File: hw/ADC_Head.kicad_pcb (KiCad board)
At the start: 2 copper layers, 10 x 22 mm, 14 parts, among them J6 SMA HEAD OUT, U8 OPA365

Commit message: Head: + wire pad on the centre line (sets the piezo position), Auselia mark on the back; manual section 10 (questions and answers), clearer settling graph, head front and back views; real JLCPCB quotes noted
Co-Authored-By: Claude Sonnet 5.5 <noreply@anthropic.com>
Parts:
- moved TP1 2.40 mm to (105.0, 103.6)
- moved TP2 1.00 mm to (108.4, 103.6)
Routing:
- net HSUM: track 14.0 -> 27.1 mm, vias 0 -> 2
- net HOUT: track 16.6 -> 6.71 mm, vias 2 -> 0
- net HREF: track 25.3 -> 18.3 mm, vias 0 -> 2
- net HGND: track 11.2 -> 14.3 mm
- net HV: track 17.4 -> 18.3 mm
- net HLINE: track 21.6 -> 22.4 mm
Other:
- board text added: "+ centre"
- board text removed: "+"
- board text removed: "PZT"

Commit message: Power: 5-pin SMU header J7 replaces JP2/JP4/JP5/JP6 and the 2-pin header; top silkscreen with TP and IC numbers; slides and README updated
Co-Authored-By: Claude Sonnet 5.5 <noreply@anthropic.com>
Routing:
- net HGND: vias 6 -> 7
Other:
- board text added: "TP1"
- board text added: "TP2"
- board text added: "U8"
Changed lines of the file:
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@@
 		(layer "Edge.Cuts")
+	)
+	(gr_text "U8"
+		(at 101.872 110.5 0)
+		(layer "F.SilkS")
+		(effects
+			(font
+				(size 0.8 0.8)
+				(thickness 0.12)
+			)
+		)
+	)
+	(gr_text "TP1"
+		(at 101.9 103.6 0)
+		(layer "F.SilkS")
+		(effects
+			(font
+				(size 0.8 0.8)
+				(thickness 0.12)
+			)
+		)
+	)
+	(gr_text "TP2"
+		(at 108.3 106 0)
+		(layer "F.SilkS")
+		(effects
+			(font
+				(size 0.8 0.8)
+				(thickness 0.12)
+			)
+		)
 	)
 	(gr_text "+ centre"
@@
 		(size 0.6)
 		(drill 0.3)
+		(layers "F.Cu" "B.Cu")
+		(net "HGND")
+	)
+	(via
+		(at 108.237499 105.331537)
+		(size 0.6)
+		(drill 0.3)

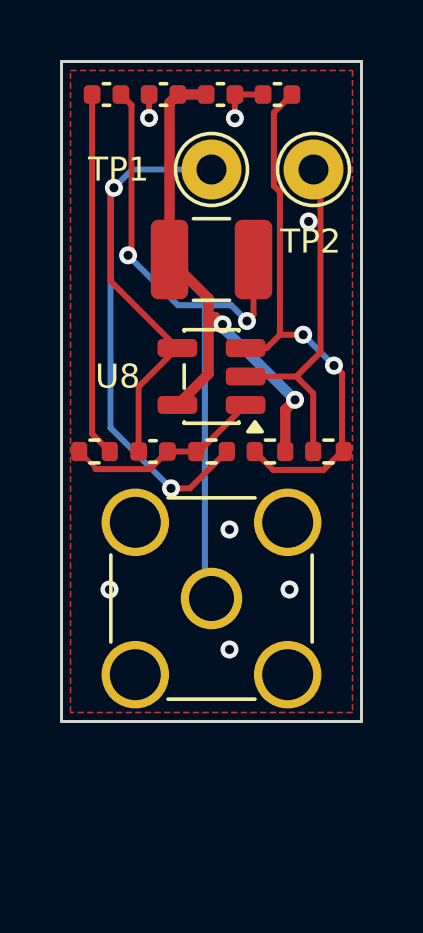
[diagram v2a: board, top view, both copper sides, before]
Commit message: Head: two M2 mounting holes (board 10 x 27 mm); JLC CPL: J7 rotation 0 and centre offset, J3 centre offset
Co-Authored-By: Claude Sonnet 5.5 <noreply@anthropic.com>
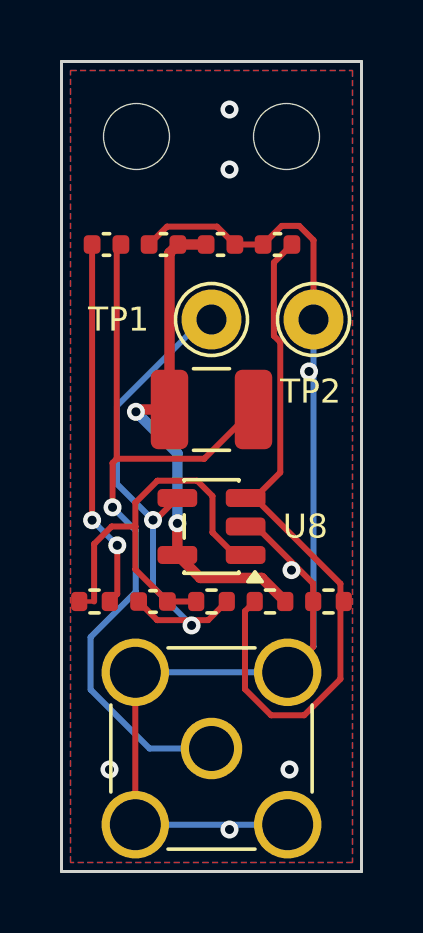
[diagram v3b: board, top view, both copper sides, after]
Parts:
- added H3: M2, MountingHole:MountingHole_2.2mm_M2, F.Cu at (102.5, 102.5)
- added H4: M2, MountingHole:MountingHole_2.2mm_M2, F.Cu at (107.5, 102.5)
- R29, R30: value 10k -> 1M
- moved C34 5.00 mm to (103.0, 118.0)
- moved C35 5.00 mm to (107.2, 106.1)
- moved C36 5.00 mm to (103.4, 106.1)
- moved C37 5.00 mm to (105.3, 106.1)
- moved C38 5.00 mm to (101.5, 106.1)
- moved J6 5.00 mm to (105.0, 122.9)
- moved L1 5.00 mm to (105.0, 111.6)
- moved R28 5.00 mm to (105.0, 118.0)
- moved R29 5.00 mm to (107.0, 118.0)
- moved R30 5.00 mm to (108.9, 118.0)
- moved R31 5.00 mm to (101.1, 118.0)
- moved TP1 5.00 mm to (105.0, 108.6)
- moved TP2 5.00 mm to (108.4, 108.6)
- moved U8 5.00 mm to (105.0, 115.5)
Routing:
- net HGND: track 14.3 -> 42.8 mm
- net HSUM: track 27.1 -> 17.4 mm
- net HOUT: track 6.71 -> 14.4 mm
- net HREF: track 18.3 -> 23.9 mm, vias 2 -> 0
- net HLINE: track 22.4 -> 26.0 mm, vias 2 -> 1
- net HV: track 18.3 -> 17.3 mm
- net HAC: track 12.1 -> 12.4 mm, vias 0 -> 2
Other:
- board size 10 x 22 mm -> 10 x 27 mm

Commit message: Head: +/- silk, U8 CPL rotation 0; main board silk says v1
Co-Authored-By: Claude Sonnet 5.5 <noreply@anthropic.com>
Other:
- board text added: "+"
- board text removed: "TP1"
- board text removed: "TP2"
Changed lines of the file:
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@@
 		(layer "Edge.Cuts")
 	)
-	(gr_text "TP1"
-		(at 101.9 108.6 0)
+	(gr_text "U8"
+		(at 103.226 115.5 0)
 		(layer "F.SilkS")
 		(effects
@@
 		)
 	)
-	(gr_text "U8"
-		(at 108.128 115.5 0)
+	(gr_text "+"
+		(at 102.2 108.6 0)
 		(layer "F.SilkS")
 		(effects
 			(font
-				(size 0.8 0.8)
-				(thickness 0.12)
+				(size 1.2 1.2)
+				(thickness 0.18)
 			)
 		)
 	)
-	(gr_text "TP2"
-		(at 108.3 111 0)
+	(gr_text "-"
+		(at 108.4 111.2 0)
 		(layer "F.SilkS")
 		(effects
 			(font
-				(size 0.8 0.8)
-				(thickness 0.12)
+				(size 1.2 1.2)
+				(thickness 0.18)
 			)
 		)
